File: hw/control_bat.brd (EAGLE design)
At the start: 92.7 x 30.5 mm, 5 parts, among them X1 DF13-4P-1.25V(50)

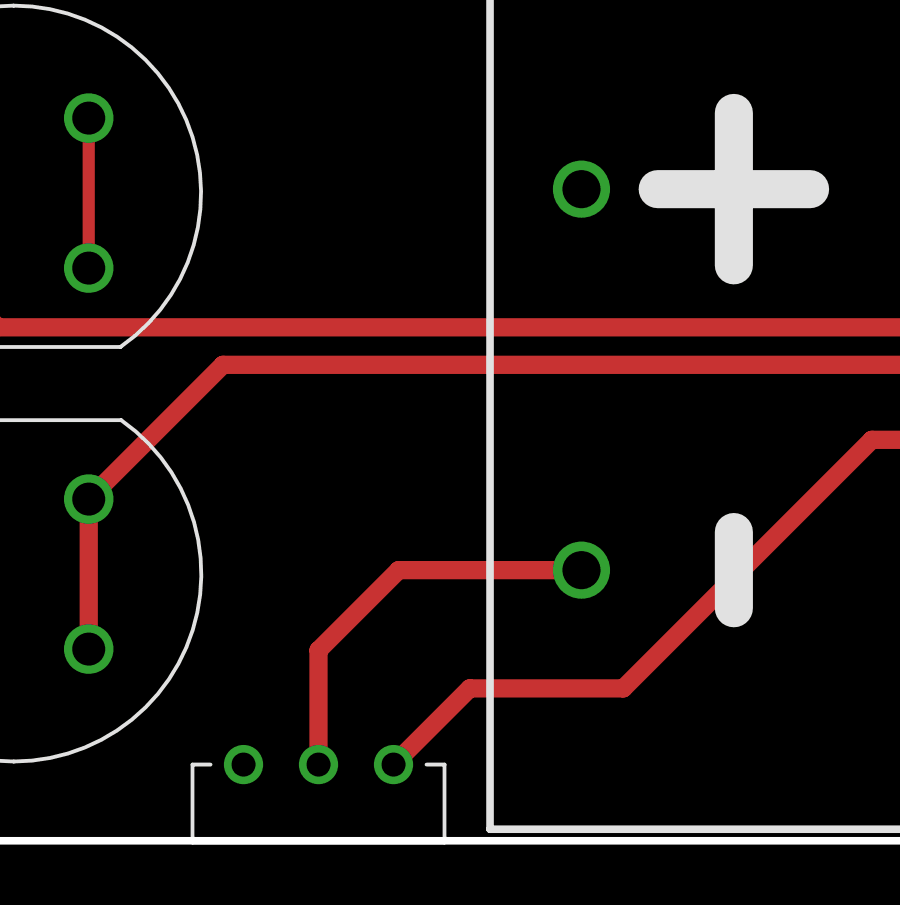
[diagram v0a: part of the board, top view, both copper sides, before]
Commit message: Fix battery orientation in control board. Panelize for manufacturing.
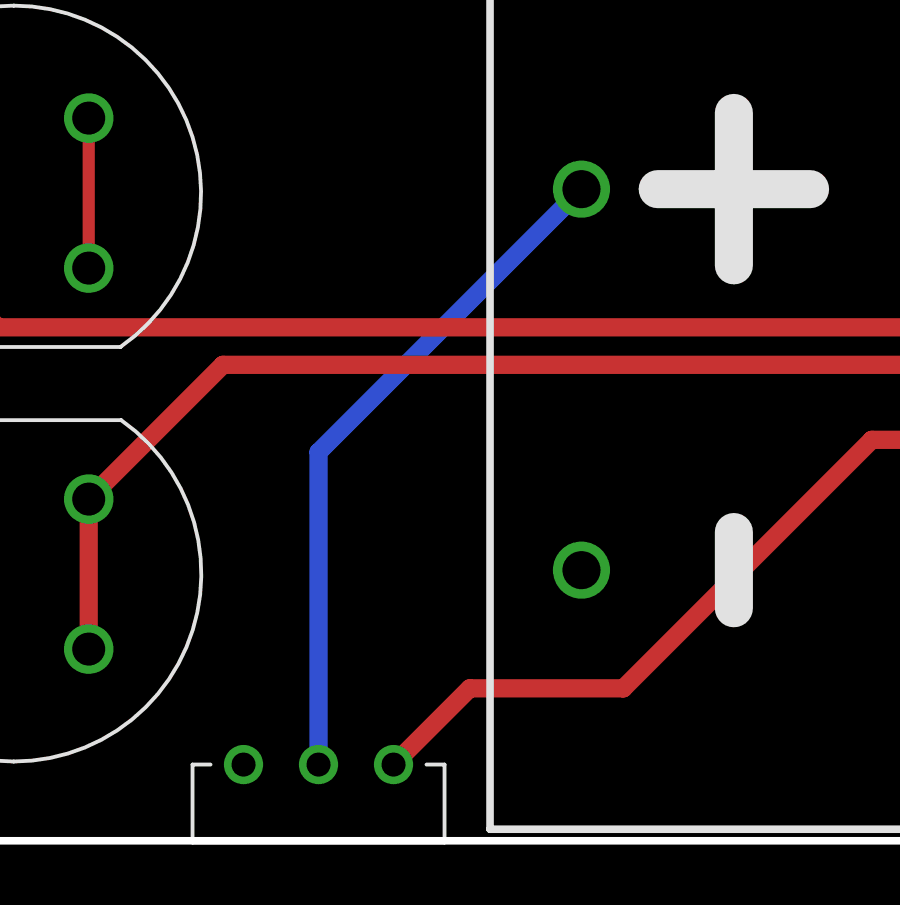
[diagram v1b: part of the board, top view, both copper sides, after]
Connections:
- net GND: now also G1.N; no longer G1.P
- net N$4: now also G1.P; no longer G1.N
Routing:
- net N$4: track 13.7 -> 22.8 mm
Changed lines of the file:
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@@
 <vertex x="0" y="0"/>
 </polygon>
-<contactref element="G1" pad="P"/>
+<contactref element="G1" pad="N"/>
 </signal>
 <signal name="VIN">
@@
 <signal name="N$4">
 <contactref element="S3" pad="P$2"/>
-<wire x1="20.32" y1="2.54" x2="20.32" y2="6.35" width="0.6096" layer="1"/>
-<wire x1="20.32" y1="6.35" x2="22.991" y2="9.021" width="0.6096" layer="1"/>
-<contactref element="G1" pad="N"/>
-<wire x1="22.991" y1="9.021" x2="29.085" y2="9.021" width="0.6096" layer="1"/>
+<contactref element="G1" pad="P"/>
+<wire x1="29.085" y1="21.721" x2="20.32" y2="12.956" width="0.6096" layer="16"/>
+<wire x1="20.32" y1="12.956" x2="20.32" y2="2.54" width="0.6096" layer="16"/>
 </signal>
 </signals>
